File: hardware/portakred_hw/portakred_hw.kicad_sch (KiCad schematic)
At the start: 0 parts

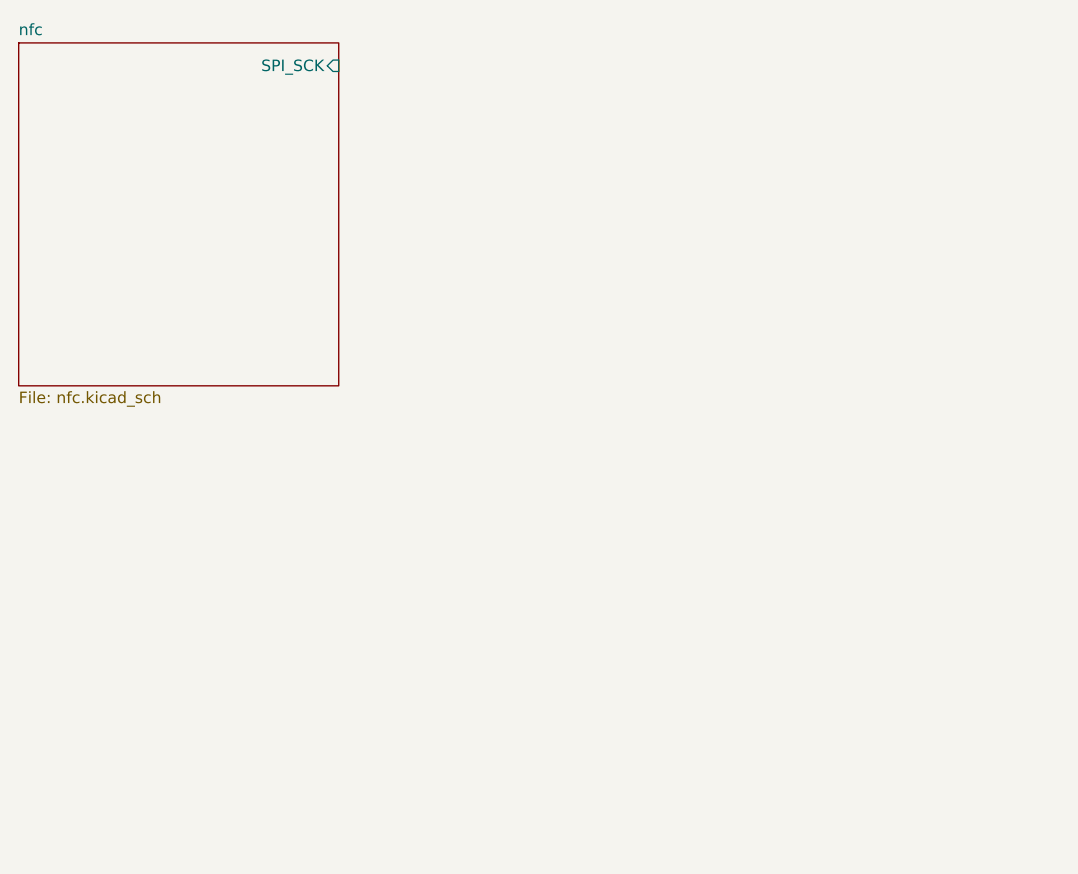
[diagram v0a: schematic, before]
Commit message: Added  Keypad sheet Added Core sheet
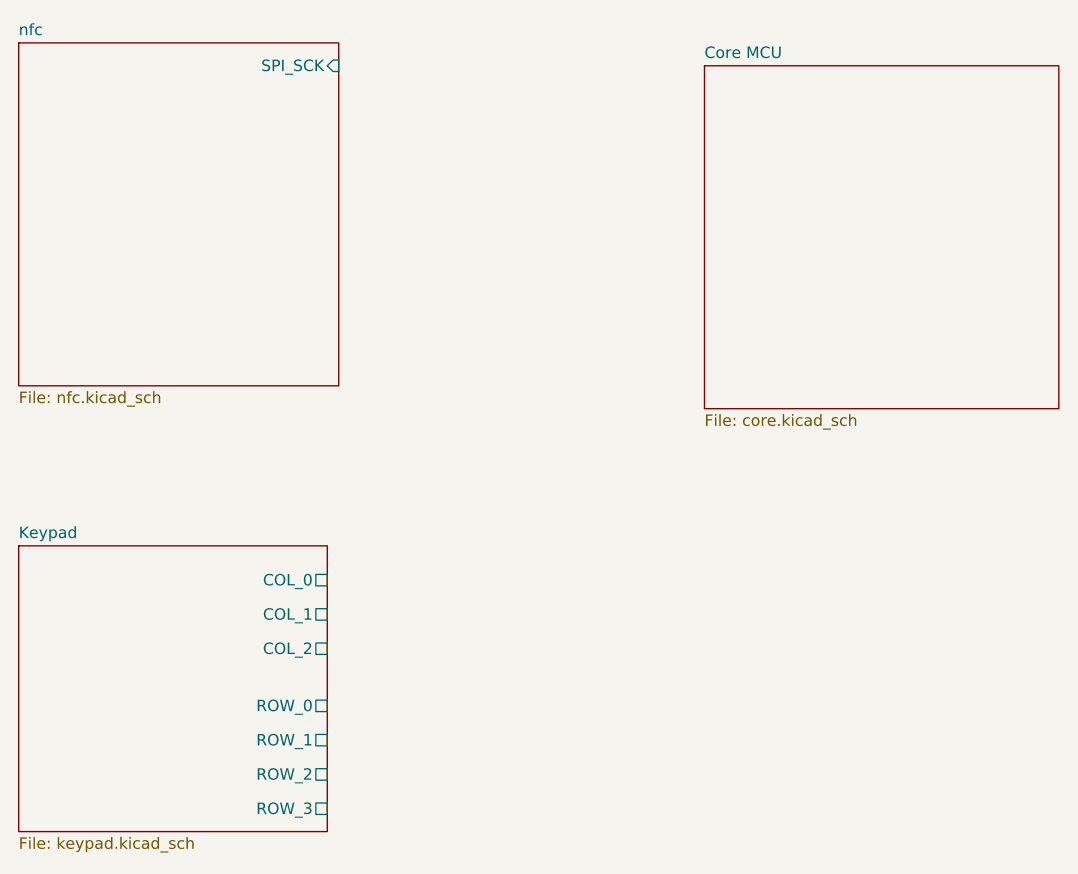
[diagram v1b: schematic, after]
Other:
- added sheet Core MCU (core.kicad_sch)
- added sheet Keypad (keypad.kicad_sch)
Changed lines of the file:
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@@
+    )
+  )
+  (sheet (at 43.18 93.98) (size 34.29 31.75) (fields_autoplaced)
+    (stroke (width 0.1524) (type solid))
+    (fill (color 0 0 0 0.0000))
+    (property "Sheetname" "Keypad" (at 43.18 93.2684 0)
+      (effects (font (size 1.27 1.27)) (justify left bottom))
+    )
+    (property "Sheetfile" "keypad.kicad_sch" (at 43.18 126.3146 0)
+      (effects (font (size 1.27 1.27)) (justify left top))
+    )
+    (pin "COL_2" passive (at 77.47 105.41 0)
+      (effects (font (size 1.27 1.27)) (justify right))
+    )
+    (pin "ROW_0" passive (at 77.47 111.76 0)
+      (effects (font (size 1.27 1.27)) (justify right))
+    )
+    (pin "ROW_3" passive (at 77.47 123.19 0)
+      (effects (font (size 1.27 1.27)) (justify right))
+    )
+    (pin "ROW_1" passive (at 77.47 115.57 0)
+      (effects (font (size 1.27 1.27)) (justify right))
+    )
+    (pin "ROW_2" passive (at 77.47 119.38 0)
+      (effects (font (size 1.27 1.27)) (justify right))
+    )
+    (pin "COL_1" passive (at 77.47 101.6 0)
+      (effects (font (size 1.27 1.27)) (justify right))
+    )
+    (pin "COL_0" passive (at 77.47 97.79 0)
+      (effects (font (size 1.27 1.27)) (justify right))
+    )
+    (instances
+      (project "portakred_hw"
+        (path "/1dee0f9b-e94c-4c98-8bc3-fa32a62d3b75" (page "3"))
+      )
+    )
+  )
+  (sheet (at 119.38 40.64) (size 39.37 38.1) (fields_autoplaced)
+    (stroke (width 0.1524) (type solid))
+    (fill (color 0 0 0 0.0000))
+    (property "Sheetname" "Core MCU" (at 119.38 39.9284 0)
+      (effects (font (size 1.27 1.27)) (justify left bottom))
+    )
+    (property "Sheetfile" "core.kicad_sch" (at 119.38 79.3246 0)
+      (effects (font (size 1.27 1.27)) (justify left top))
+    )
+    (instances
+      (project "portakred_hw"
+        (path "/1dee0f9b-e94c-4c98-8bc3-fa32a62d3b75" (page "4"))
+      )
     )
   )

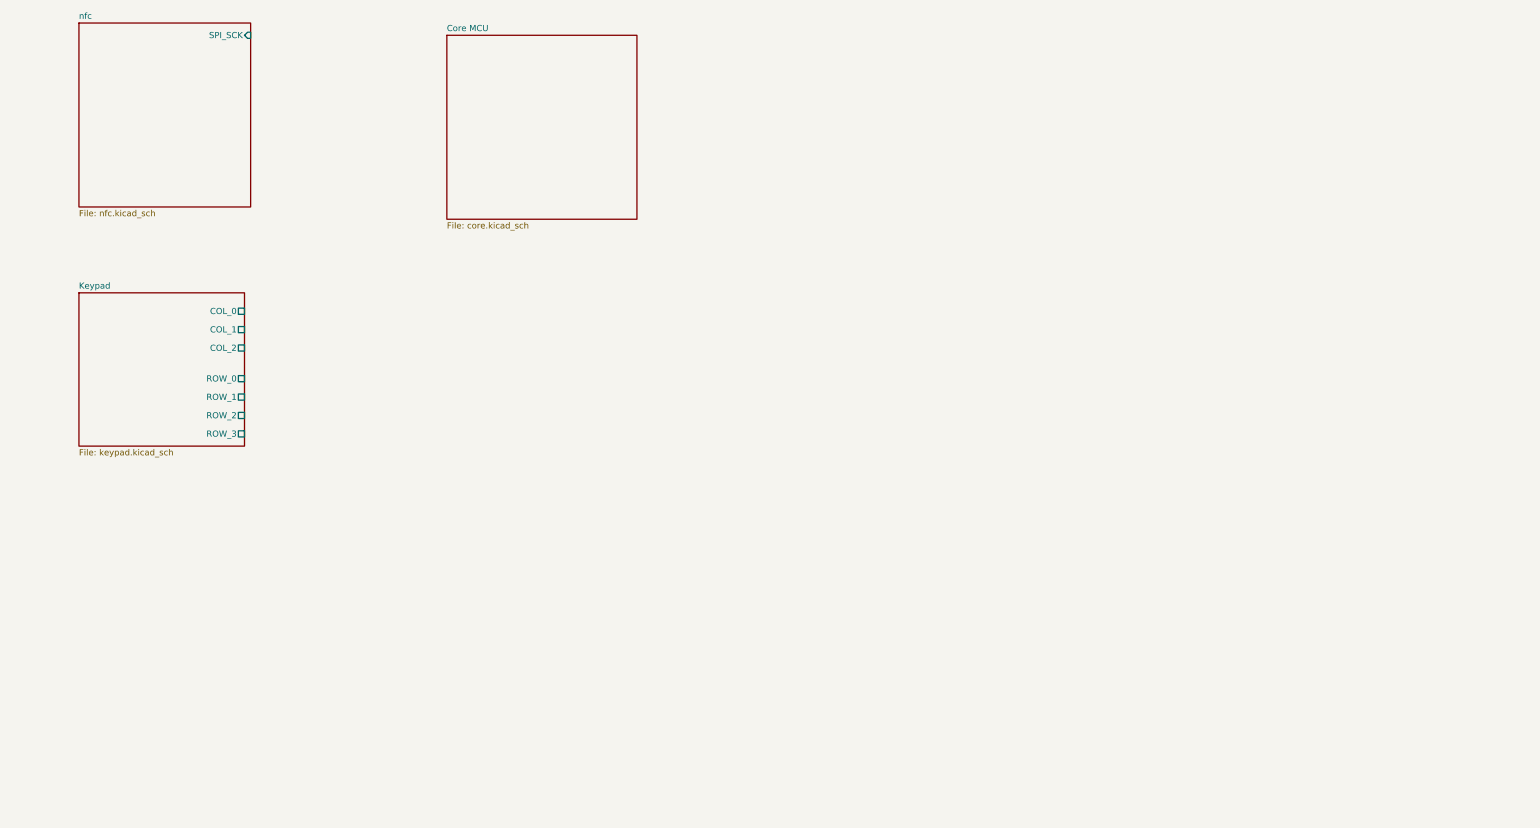
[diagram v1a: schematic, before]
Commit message: Progress on core circuitry, moved core to root sheet, fix broken library dependency
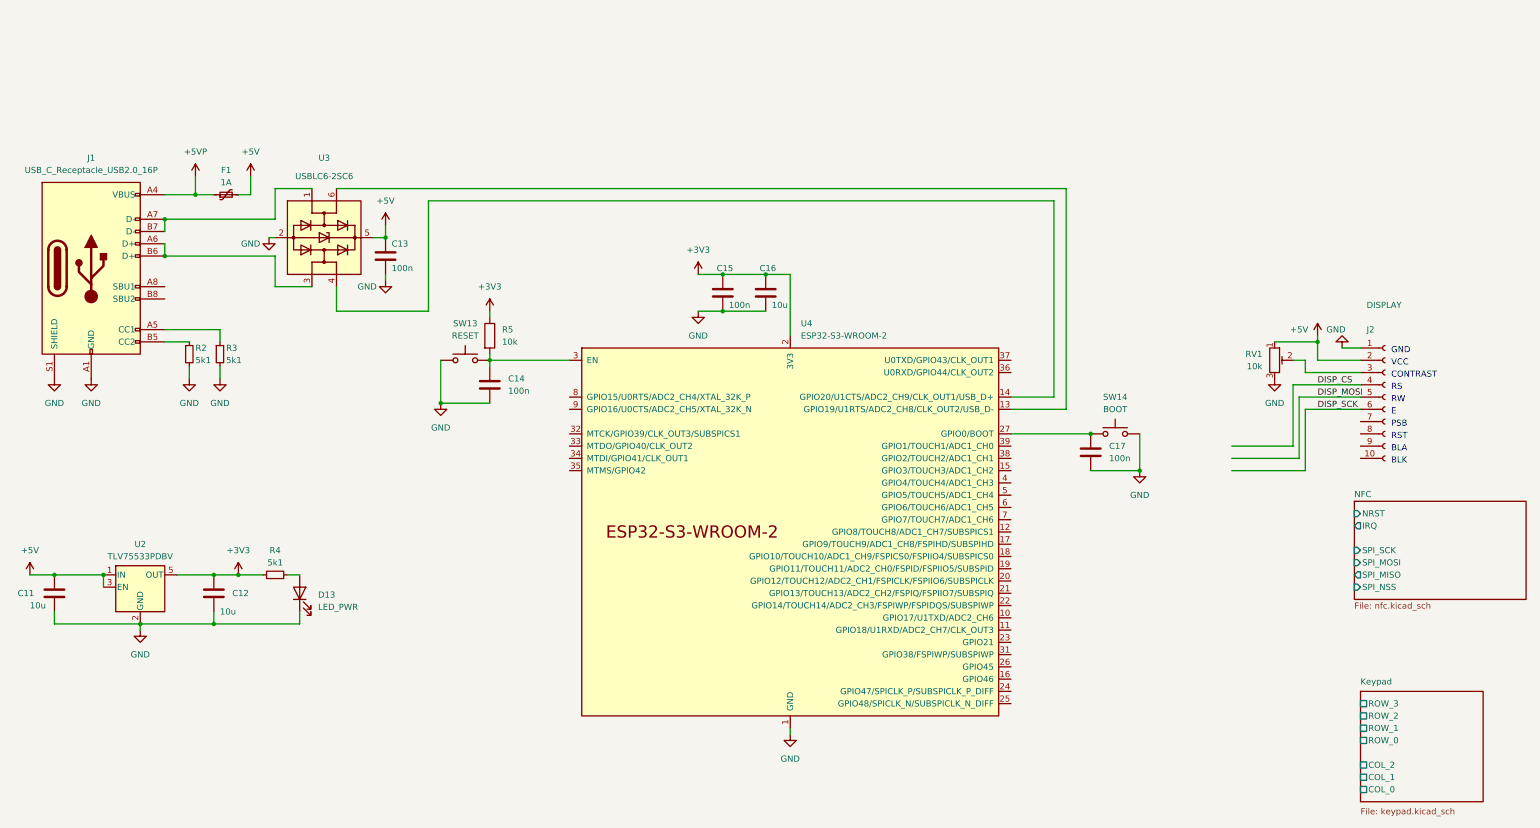
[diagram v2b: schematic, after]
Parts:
- added C11, C12, C16: 10u, symbol Device:C
- added C13, C14, C15, C17: 100n, symbol Device:C
- added D13: LED_PWR, symbol Device:LED
- added F1: 1A, symbol Device:Polyfuse_Small
- added J1: USB_C_Receptacle_USB2.0_16P, symbol Connector:USB_C_Receptacle_USB2.0_16P
- added J2: DISPLAY, symbol Connector:Conn_01x10_Socket
- added R2, R3, R4: 5k1, symbol Device:R_Small
- added R5: 10k, symbol Device:R
- added RV1: 10k, symbol Device:R_Potentiometer_Trim
- added SW13: RESET, symbol Switch:SW_Push
- added SW14: BOOT, symbol Switch:SW_Push
- added U2: TLV75533PDBV, Package_TO_SOT_SMD:SOT-23-5, symbol Regulator_Linear:TLV75533PDBV
- added U3: USBLC6-2SC6, Package_TO_SOT_SMD:SOT-23-6, symbol Power_Protection:USBLC6-2SC6
- added U4: ESP32-S3-WROOM-2, PCM_Espressif:ESP32-S3-WROOM-2, symbol PCM_Espressif:ESP32-S3-WROOM-2
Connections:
- new net: C14.1, R5.2, SW13.2, U4.3 (EN)
- new net: C17.1, SW14.1, U4.27 (GPIO0/BOOT)
- new net: J2.3 (Pin_3), RV1.2
- new net: U3.6 (I/O1), U4.13 (GPIO19/U1RTS/ADC2_CH8/CLK_OUT2/USB_D-)
- new net: U3.4 (I/O2), U4.14 (GPIO20/U1CTS/ADC2_CH9/CLK_OUT1/USB_D+)
- new net: D13.2 (A), R4.2
- new net: J1.A5 (CC1), R3.1
- new net: J1.A6 (D+), J1.B6 (D+), U3.3 (I/O2)
- new net: J1.A7 (D-), J1.B7 (D-), U3.1 (I/O1)
- new net: J1.B5 (CC2), R2.1
- new net +3V3: C12.1, C15.1, C16.1, R4.1, R5.1, U2.5 (OUT), U4.2 (3V3)
- new net +5V: C11.1, C13.1, F1.2, J2.2 (Pin_2), RV1.1, U2.1 (IN), U2.3 (EN), U3.5 (VBUS)
- new net +5VP: F1.1, J1.A4 (VBUS), J1.A9 (VBUS), J1.B4 (VBUS), J1.B9 (VBUS)
- new net DISP_CS: J2.4 (Pin_4)
- new net DISP_MOSI: J2.5 (Pin_5)
- new net DISP_SCK: J2.6 (Pin_6)
- new net GND: C11.2, C12.2, C13.2, C14.2, C15.2, C16.2, C17.2, D13.1 (K), J1.A1 (GND), J1.A12 (GND), J1.B1 (GND), J1.B12 (GND), J1.S1 (SHIELD), J2.1 (Pin_1), R2.2, R3.2, RV1.3, SW13.1, SW14.2, U2.2 (GND), U3.2 (GND), U4.1 (GND), U4.40 (GND), U4.41 (GND)
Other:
- sheet nfc renamed NFC
- removed sheet Core MCU
- sheet NFC ports: added IRQ, NRST, SPI_MISO, SPI_MOSI, SPI_NSS; removed none
- note added: "BLA"
- note added: "BLK"
- note added: "CONTRAST"
- note added: "E"
- note added: "GND"
- note added: "PSB"
- note added: "RS"
- note added: "RST"
- note added: "RW"
- note added: "VCC"

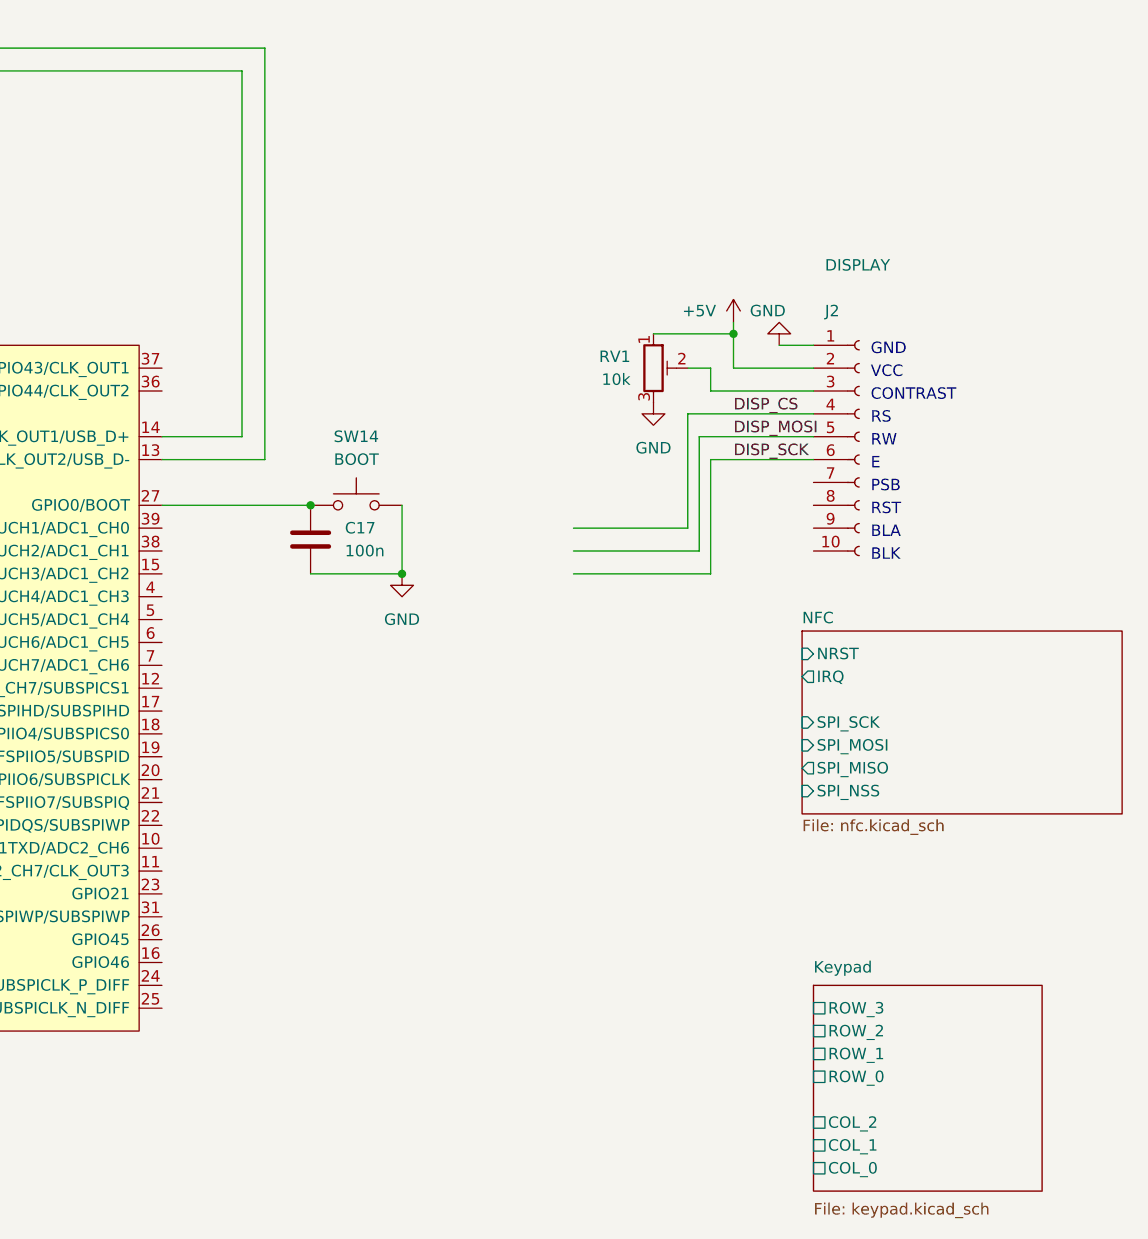
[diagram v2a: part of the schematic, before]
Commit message: Connected peripherals to ESP, Added NFC antenna circuitry, added buzzer
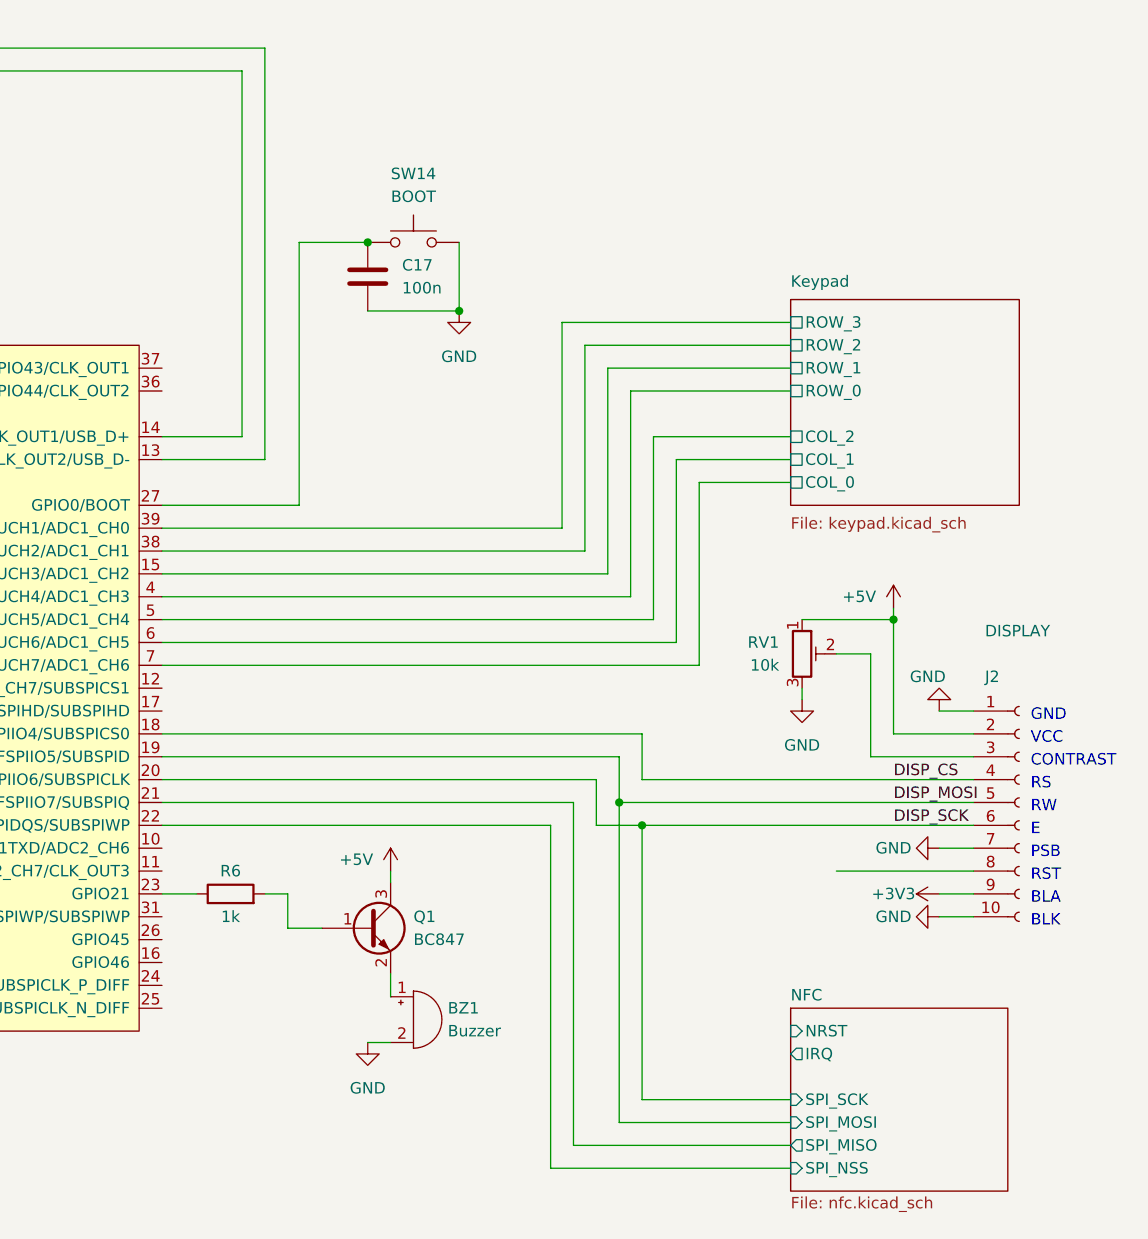
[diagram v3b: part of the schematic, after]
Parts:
- added BZ1: Buzzer, Buzzer_Beeper:Buzzer_15x7.5RM7.6, symbol Device:Buzzer
- added Q1: BC847, Package_TO_SOT_SMD:SOT-23, symbol Transistor_BJT:BC847
- added R6: 1k, symbol Device:R
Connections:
- net +3V3: now also J2.9 (Pin_9)
- net +5V: now also Q1.3 (C)
- net DISP_CS: now also U4.18 (GPIO10/TOUCH10/ADC1_CH9/FSPICS0/FSPIIO4/SUBSPICS0)
- net DISP_MOSI: now also U4.19 (GPIO11/TOUCH11/ADC2_CH0/FSPID/FSPIIO5/SUBSPID)
- net DISP_SCK: now also U4.20 (GPIO12/TOUCH12/ADC2_CH1/FSPICLK/FSPIIO6/SUBSPICLK)
- net GND: now also J2.10 (Pin_10), J2.7 (Pin_7), BZ1.2 (-)
- net Keypad/COL_0: now also U4.7 (GPIO7/TOUCH7/ADC1_CH6)
- net Keypad/COL_1: now also U4.6 (GPIO6/TOUCH6/ADC1_CH5)
- net Keypad/COL_2: now also U4.5 (GPIO5/TOUCH5/ADC1_CH4)
- net Keypad/ROW_0: now also U4.4 (GPIO4/TOUCH4/ADC1_CH3)
- net Keypad/ROW_1: now also U4.15 (GPIO3/TOUCH3/ADC1_CH2)
- net Keypad/ROW_2: now also U4.38 (GPIO2/TOUCH2/ADC1_CH1)
- net Keypad/ROW_3: now also U4.39 (GPIO1/TOUCH1/ADC1_CH0)
- net NFC/SPI_MISO: now also U4.21 (GPIO13/TOUCH13/ADC2_CH2/FSPIQ/FSPIIO7/SUBSPIQ)
- net NFC/SPI_NSS: now also U4.22 (GPIO14/TOUCH14/ADC2_CH3/FSPIWP/FSPIDQS/SUBSPIWP)
- net at U4.23 (GPIO21): now also R6.1
- new net: BZ1.1 (+), Q1.2 (E)
- new net: Q1.1 (B), R6.2
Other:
- moved on the sheet: C17, J2, RV1, SW14
